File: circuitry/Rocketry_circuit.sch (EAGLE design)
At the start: 17 parts, among them IC1 TC1264-3.3VAB

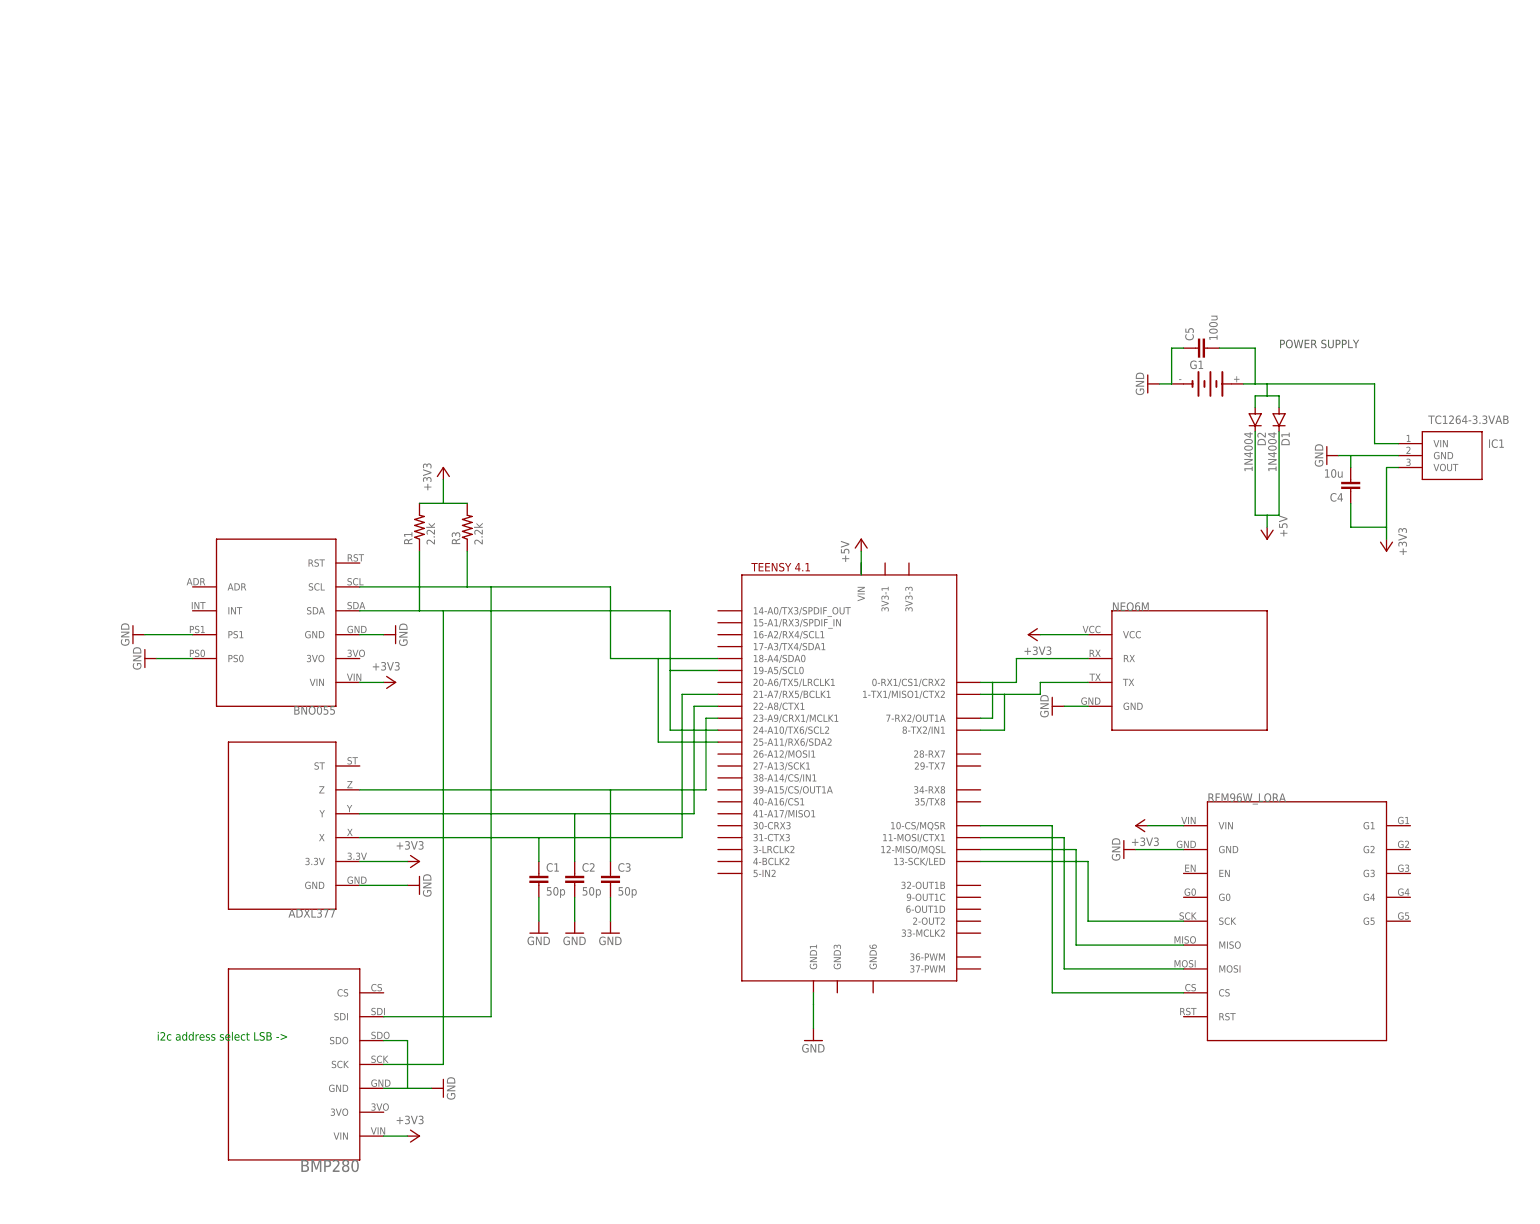
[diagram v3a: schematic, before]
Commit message: Incremental progress - 5V for GPS, interrupt wire, etc
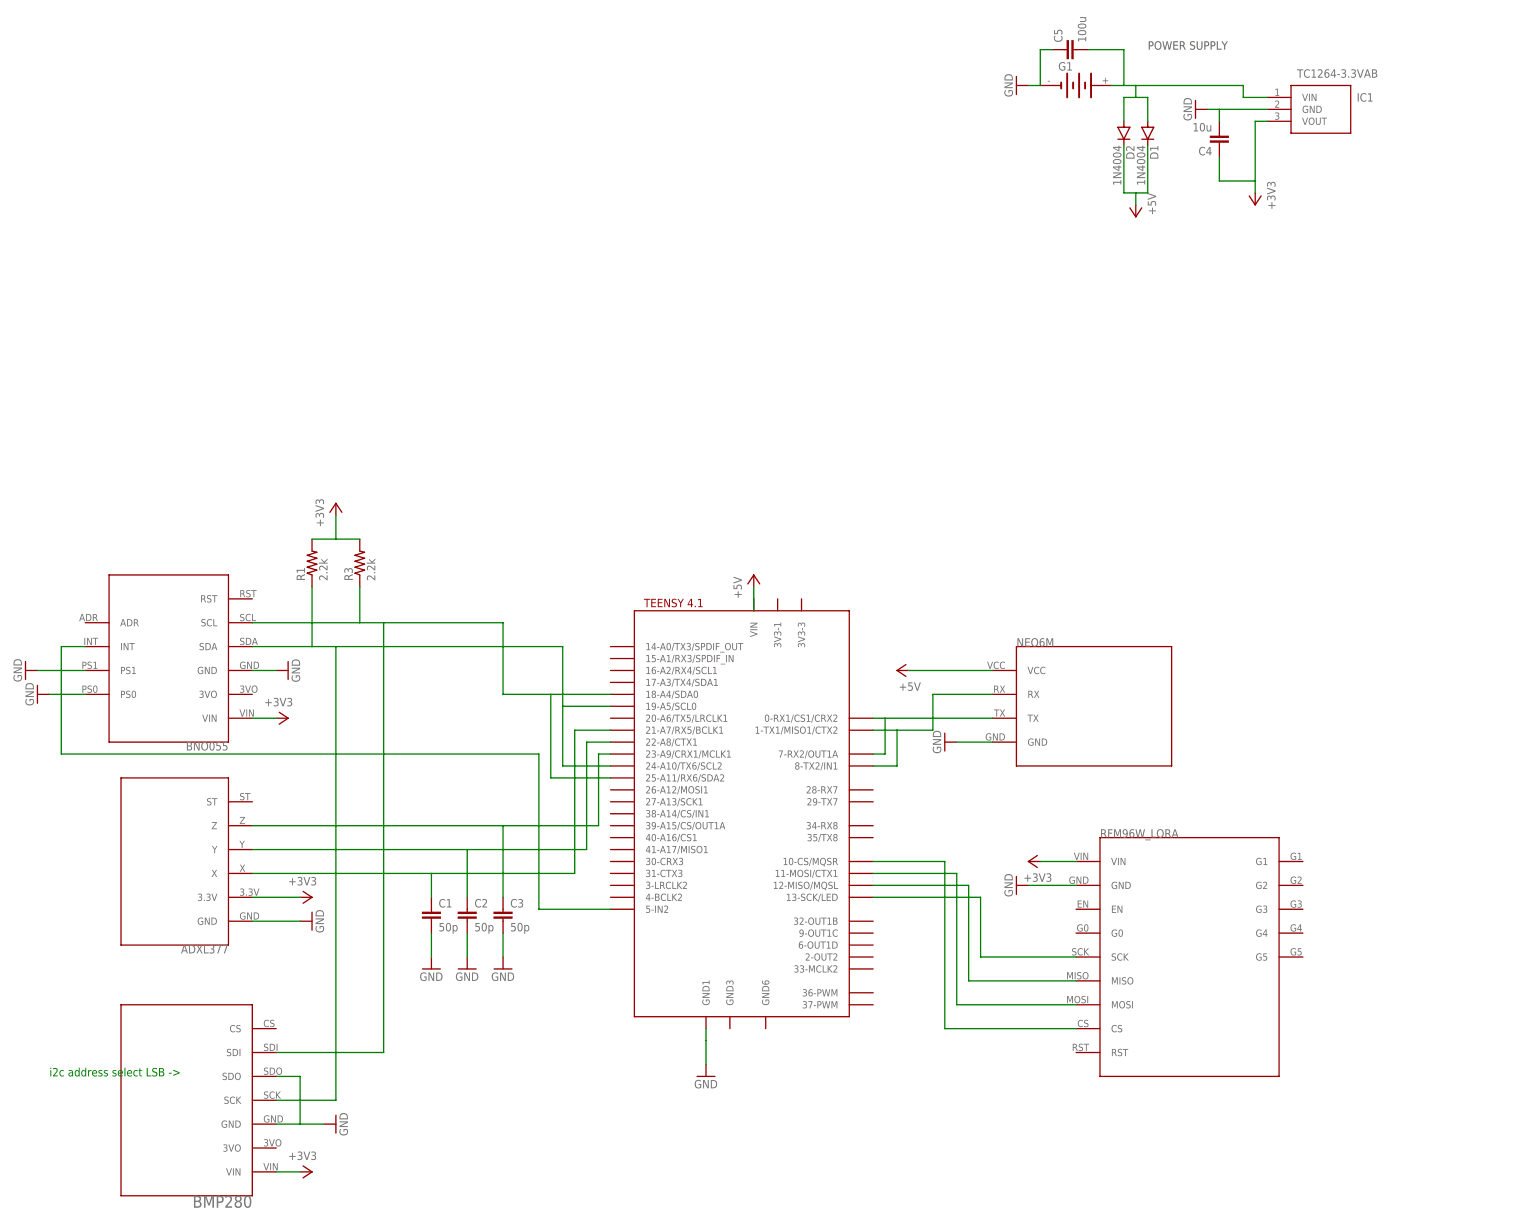
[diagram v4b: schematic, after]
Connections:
- new net N$13: BRKOUT1.INT, U$1.5-IN2
- net +3V3: no longer U$4.VCC
- net +5V: now also U$4.VCC
- net N$6: now also U$4.TX; no longer U$4.RX
- net N$7: now also U$4.RX; no longer U$4.TX
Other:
- note removed: "ONBOARD"
- moved on the sheet: C1, C2, C3, C4, C5, D1, D2, G1, IC1, R1, R3

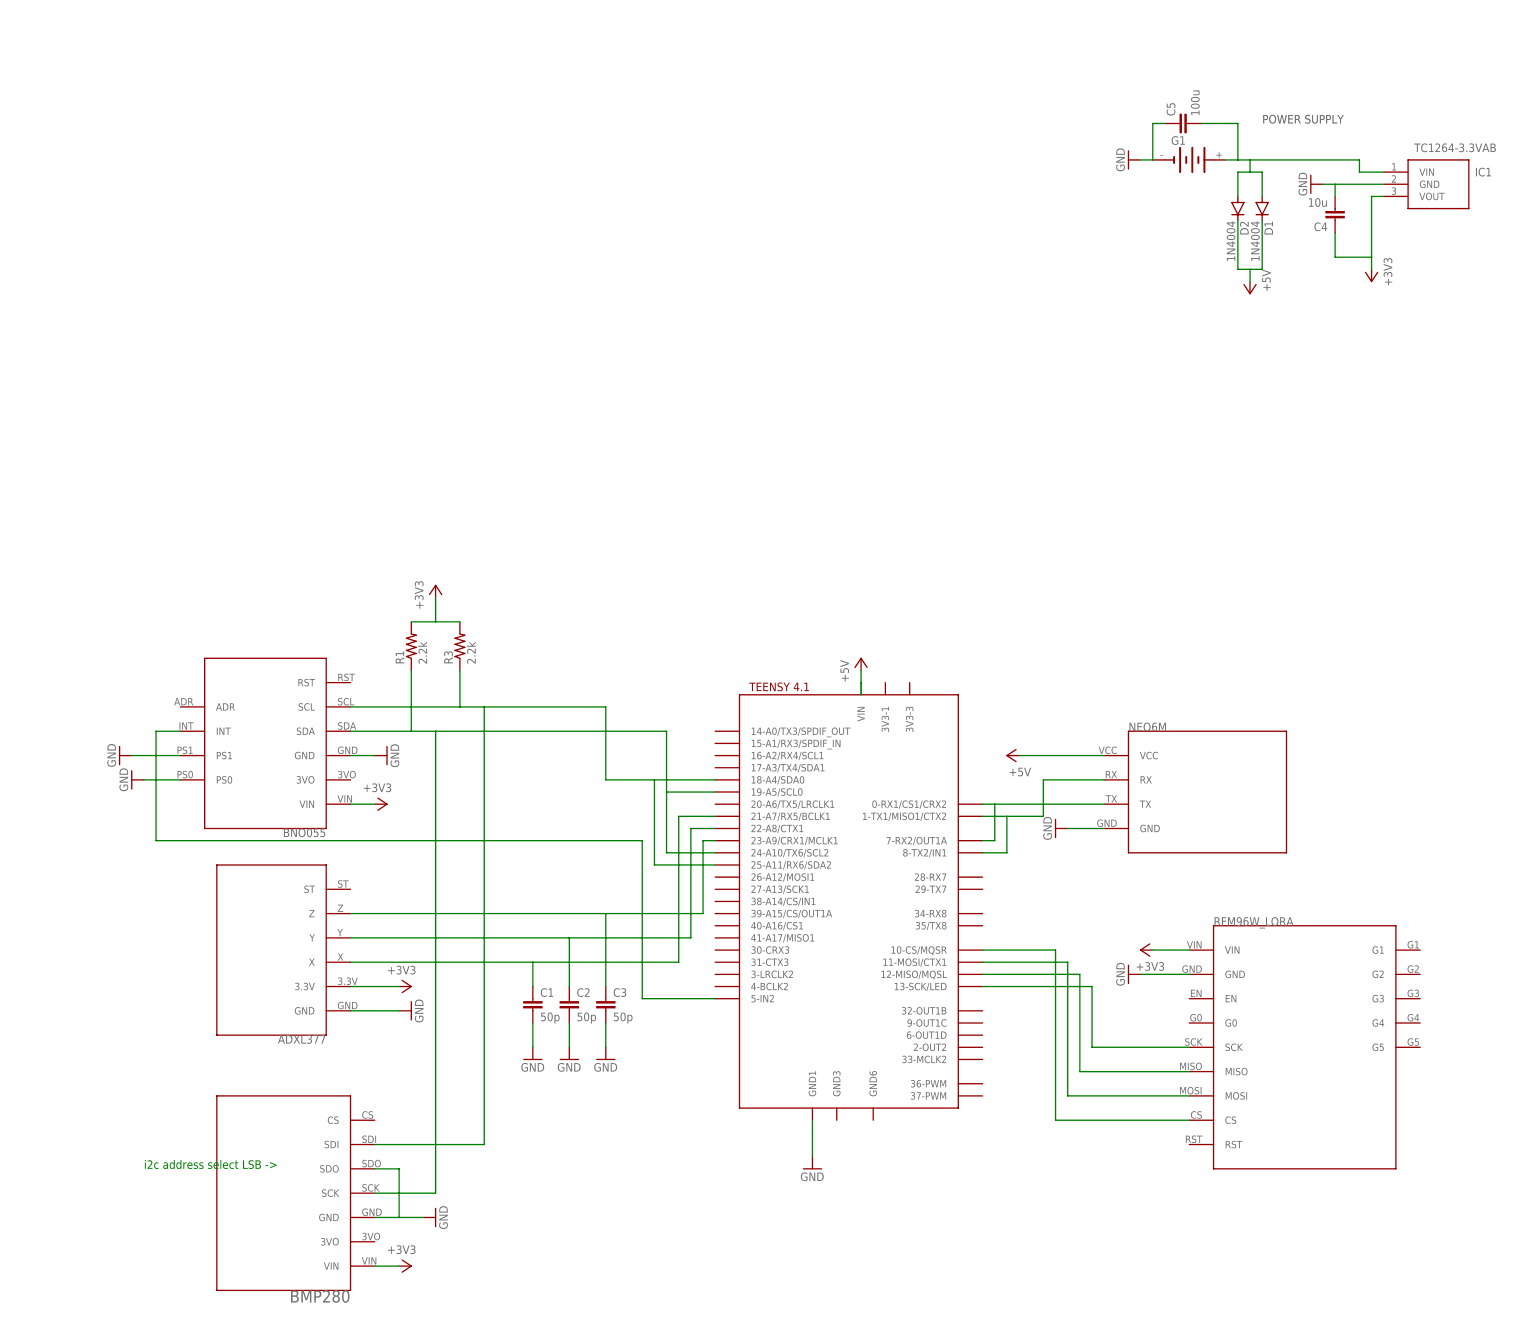
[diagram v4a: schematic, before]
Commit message: added a transisor and breakouts for spare teensy pins (incase we need them)
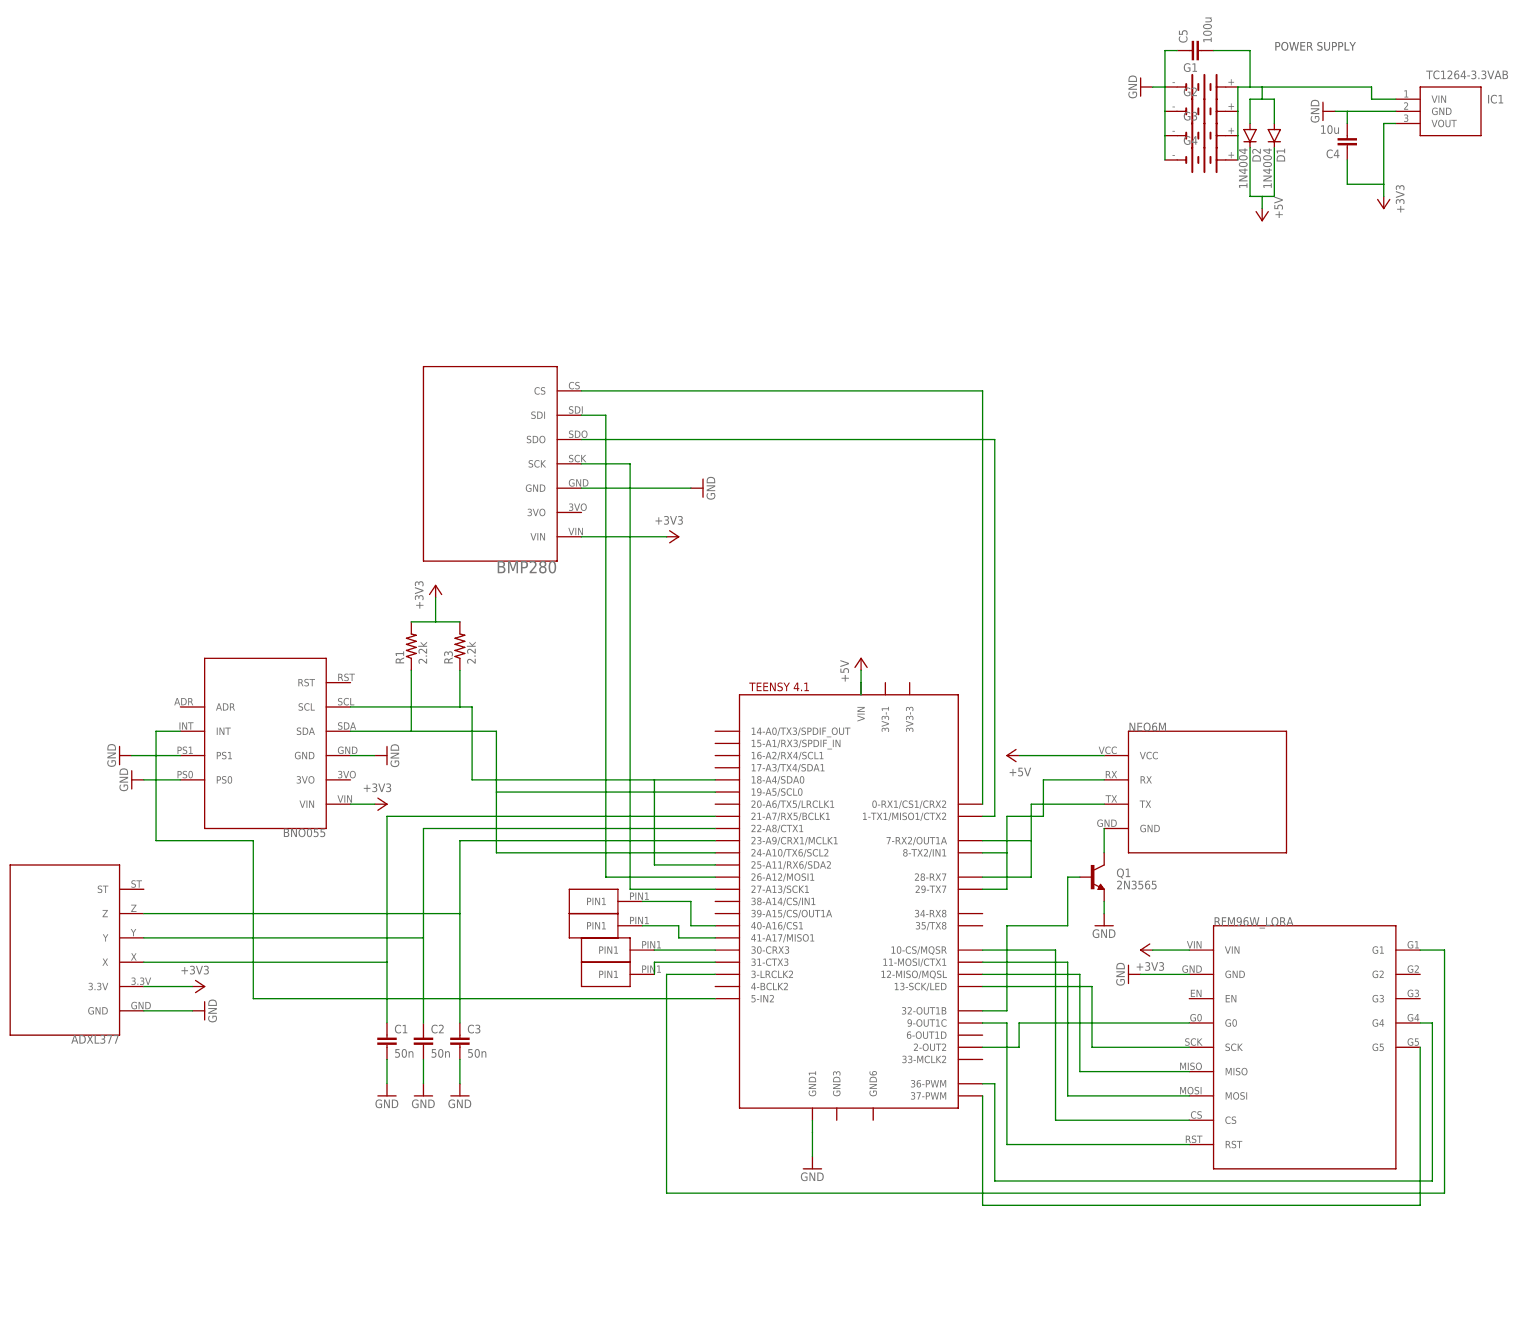
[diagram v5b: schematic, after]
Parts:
- added G2, G3, G4: 3V11R, battery:3V11R
- added Q1: 2N3565, transistor-npn:2N3565
- added U$6, U$7, U$8, U$9: 1PINOUT, 1PINOUT:1PINOUT
- C1, C2, C3: value 50p -> 50n
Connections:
- new net N$14: U$1.1-TX1/MISO1/CTX2, U$2.SDO
- new net N$15: U$1.27-A13/SCK1, U$2.SCK
- new net N$16: U$1.0-RX1/CS1/CRX2, U$2.CS
- new net N$17: U$1.26-A12/MOSI1, U$2.SDI
- new net N$18: U$1.2-OUT2, U$5.G0
- new net N$19: U$1.3-LRCLK2, U$5.G1
- new net N$20: U$1.9-OUT1C, U$5.RST
- new net N$21: U$1.36-PWM, U$5.G4
- new net N$22: U$1.37-PWM, U$5.G5
- new net N$23: Q1.B, U$1.32-OUT1B
- new net N$24: Q1.C, U$4.GND
- new net N$25: U$1.31-CTX3, U$6.PIN1
- new net N$26: U$1.41-A17/MISO1, U$7.PIN1
- new net N$27: U$1.30-CRX3, U$8.PIN1
- new net N$28: U$1.40-A16/CS1, U$9.PIN1
- net GND: now also G2.-, G3.-, G4.-, Q1.E; no longer U$2.SDO, U$4.GND
- net N$12: now also G2.+, G3.+, G4.+
- net N$3: no longer U$2.SCK
- net N$5: no longer U$2.SDI
- net N$6: now also U$1.28-RX7; no longer U$1.0-RX1/CS1/CRX2
- net N$7: now also U$1.29-TX7; no longer U$1.1-TX1/MISO1/CTX2
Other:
- note removed: "i2c address select LSB ->"
- moved on the sheet: C1, C2, C3, C4, C5, D1, D2, G1, IC1

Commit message: Final sch and brd files - Ordered pcb
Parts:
- removed G2, G3: 3V11R, battery:3V11R
- added U$10, U$11, U$13, U$14, U$15, U$16: 1PINOUT, 1PINOUT:1PINOUT
- added U$12: SMALL_SCREW_TERMINAL, SMALL_SCREW_TERMINAL:SMALL_SCREW_TERMINAL
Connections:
- removed net N$14 (its old number): U$1.1-TX1/MISO1/CTX2, U$2.SDO
- removed net N$28: U$1.40-A16/CS1, U$9.PIN1
- new net N$18: U$1.28-RX7, U$6.PIN1
- net GND: now also U$10.PIN1, U$11.PIN1, U$12.GND, U$3.ST; no longer G2.-, G3.-
- net N$10: now also U$2.SDI
- net N$11: now also U$1.37-PWM; no longer U$1.10-CS/MQSR
- net N$12: now also U$12.V+; no longer G2.+, G3.+
- net N$15: now also U$1.24-A10/TX6/SCL2, U$9.PIN1; no longer U$1.27-A13/SCK1, U$2.SCK
- net N$16: now also U$1.10-CS/MQSR; no longer U$1.0-RX1/CS1/CRX2
- net N$17: now also U$1.25-A11/RX6/SDA2, U$7.PIN1; no longer U$1.26-A12/MOSI1, U$2.SDI
- net N$21: now also U$1.29-TX7, U$8.PIN1; no longer U$1.36-PWM, U$5.G4
- net N$22: now also U$1.26-A12/MOSI1, U$13.PIN1; no longer U$1.37-PWM, U$5.G5
- net N$25: now also U$1.27-A13/SCK1, U$14.PIN1; no longer U$1.31-CTX3, U$6.PIN1
- net N$26: now also U$1.0-RX1/CS1/CRX2, U$15.PIN1; no longer U$1.41-A17/MISO1, U$7.PIN1
- net N$27: now also U$1.1-TX1/MISO1/CTX2, U$16.PIN1; no longer U$1.30-CRX3, U$8.PIN1
- net N$3: now also U$1.18-A4/SDA0; no longer U$1.19-A5/SCL0, U$1.24-A10/TX6/SCL2
- net N$5: now also U$1.19-A5/SCL0; no longer U$1.18-A4/SDA0, U$1.25-A11/RX6/SDA2
- net N$6: no longer U$1.28-RX7
- net N$7: no longer U$1.29-TX7
- net N$8: now also U$2.SCK
- net N$9: now also U$2.SDO
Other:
- moved on the sheet: C5, G1, G4, Q1
